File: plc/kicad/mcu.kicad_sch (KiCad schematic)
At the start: 53 parts, among them J1 Conn_01x03_Pin, J2 Conn_01x04_Pin, Q3 L8050QLT1G, Q4 L8050QLT1G, SW1 TSD003B08026A03, SW2 TSD003B08026A03, U10 ESP32-S3-MINI-1U, U11 BS-0601-SK-4W, U12 AHT20_C2757850, U13 CP2102N-A02-GQFN28R, U9 RV-3028-C7

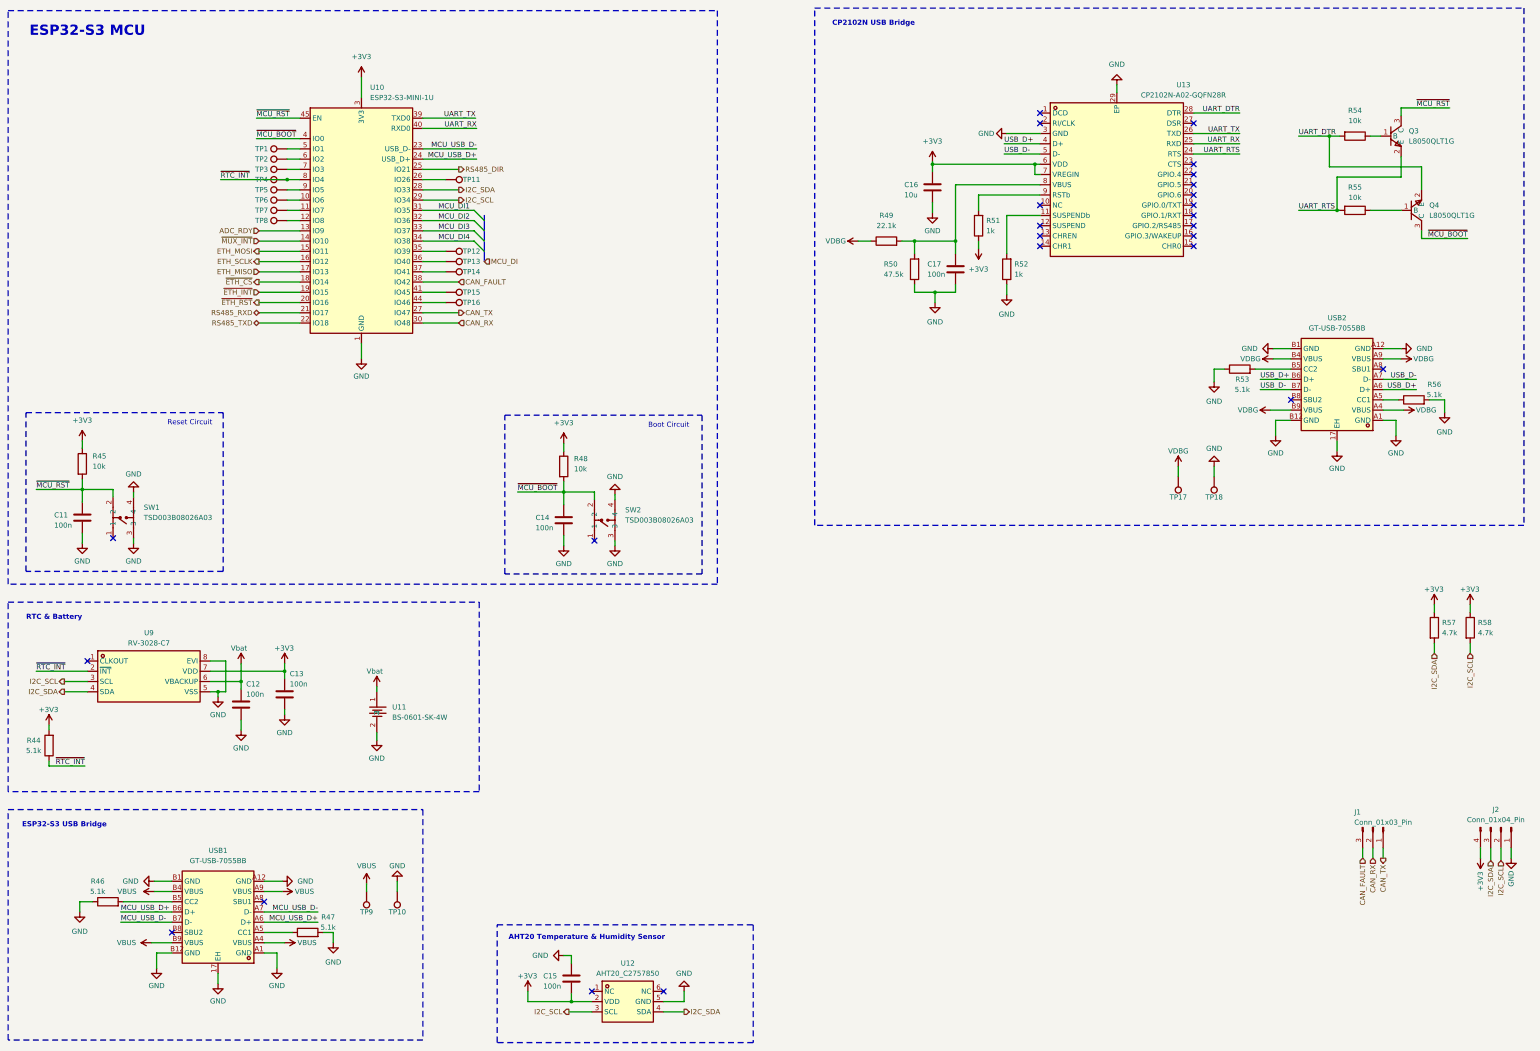
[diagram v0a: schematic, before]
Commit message: Added microSD card
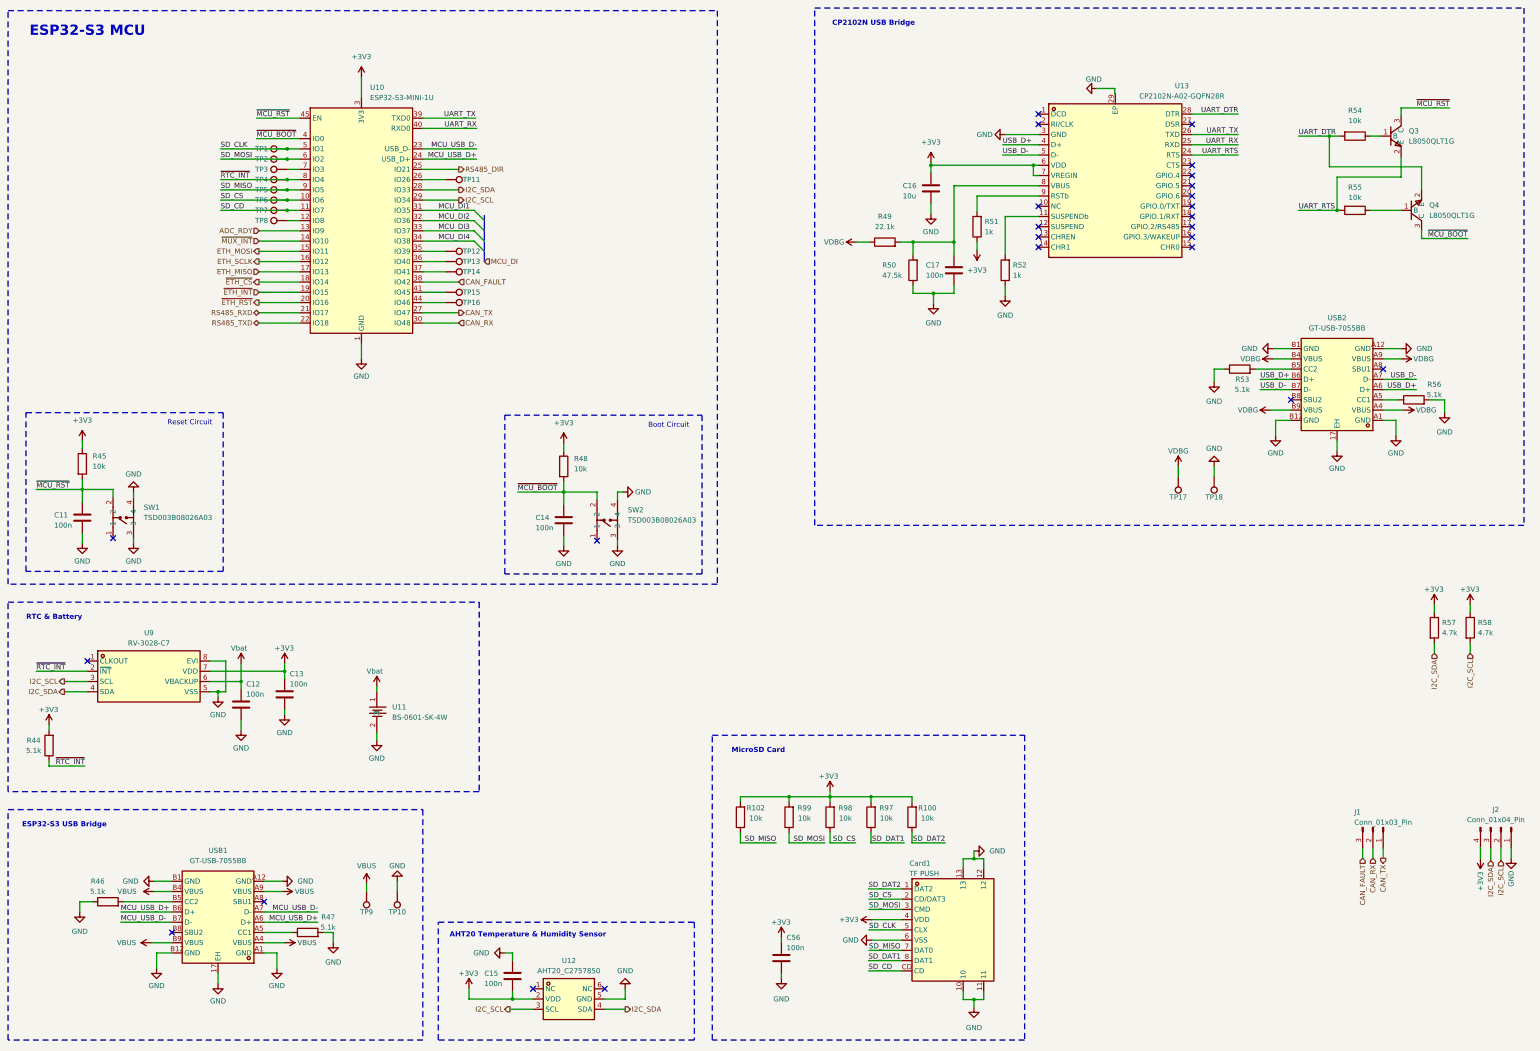
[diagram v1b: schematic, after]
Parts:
- added C56: 100n, Capacitor_SMD:C_0603_1608Metric, symbol Device:C
- added Card1: TF PUSH, LibrePLC32:TF-SMD_TF-PUSH, symbol LibrePLC32:TFPUSH
- added R100, R102, R97, R98, R99: 10k, Resistor_SMD:R_0603_1608Metric, symbol Device:R
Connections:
- net +3V3: now also C56.2, Card1.4 (VDD), R100.2, R102.2, R97.2, R98.2, R99.2
- net GND: now also C56.1, Card1.10, Card1.11, Card1.12, Card1.13, Card1.6 (VSS)
- net SD_CS: now reaches TP6.1, U10.10 (IO6)
- net SD_CS: now also Card1.2 (CD/DAT3), R98.1
- net SD_CD: now reaches TP7.1, U10.11 (IO7)
- net SD_CD: now also Card1.CD
- net SD_CLK: now reaches TP1.1, U10.5 (IO1)
- net SD_CLK: now also Card1.5 (CLX)
- net SD_MOSI: now reaches TP2.1, U10.6 (IO2)
- net SD_MOSI: now also Card1.3 (CMD), R99.1
- net SD_MISO: now reaches TP5.1, U10.9 (IO5)
- net SD_MISO: now also Card1.7 (DAT0), R102.1
- new net SD_DAT1: Card1.8 (DAT1), R97.1
- new net SD_DAT2: Card1.1 (DAT2), R100.1
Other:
- note added: "MicroSD Card"
- moved on the sheet: C15, SW2, U12

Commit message: Added setup leds & shared SPI bus
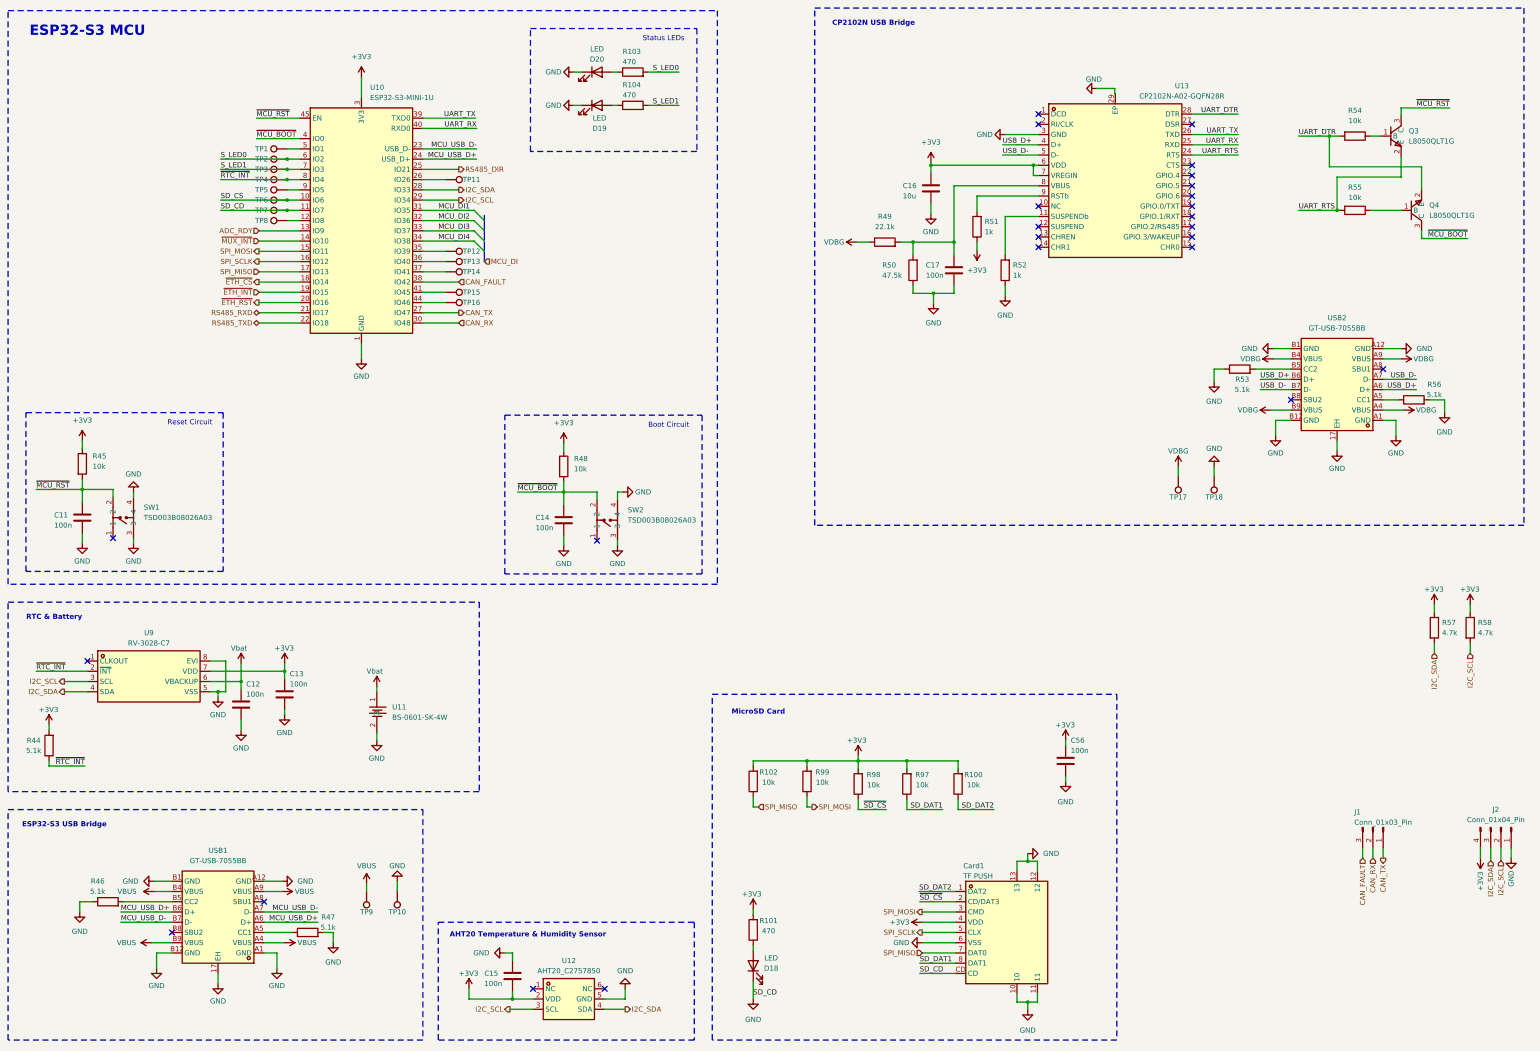
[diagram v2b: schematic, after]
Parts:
- added D18, D19, D20: LED, LED_SMD:LED_0805_2012Metric, symbol Device:LED
- added R101, R103, R104: 470, Resistor_SMD:R_0603_1608Metric, symbol Device:R
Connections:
- net SD_CD is gone; now on net GND: Card1.CD, TP7.1, U10.11 (IO7)
- net +3V3: now also R101.2
- net GND: now also D18.1 (K), D19.1 (K), D20.1 (K)
- net SD_CS: no longer Card1.2 (CD/DAT3), R98.1
- net S_LED1: now reaches TP3.1, U10.7 (IO3)
- net S_LED1: now also R104.2
- net ETH_MISO renamed SPI_MISO
- net SPI_MISO: now also Card1.7 (DAT0), R102.1
- net ETH_MOSI renamed SPI_MOSI
- net SPI_MOSI: now also Card1.3 (CMD), R99.1
- net ETH_SCLK renamed SPI_SCLK
- net SPI_SCLK: now also Card1.5 (CLX)
- net SD_CLK: no longer names the net of TP1.1, U10.5 (IO1)
- net SD_CLK: no longer Card1.5 (CLX)
- net SD_MISO: no longer names the net of TP5.1, U10.9 (IO5)
- net SD_MISO: no longer Card1.7 (DAT0), R102.1
- net SD_MOSI renamed S_LED0
- net S_LED0: now also R103.2; no longer Card1.3 (CMD), R99.1
- new net: D19.2 (A), R104.1
- new net: D18.2 (A), R101.1
- new net: D20.2 (A), R103.1
- new net ~{SD_CS}: Card1.2 (CD/DAT3), R98.1
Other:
- note added: "Status LEDs"
- moved on the sheet: C56, Card1, R100, R102, R97, R98, R99

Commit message: Fixed ADC pins & rc filter
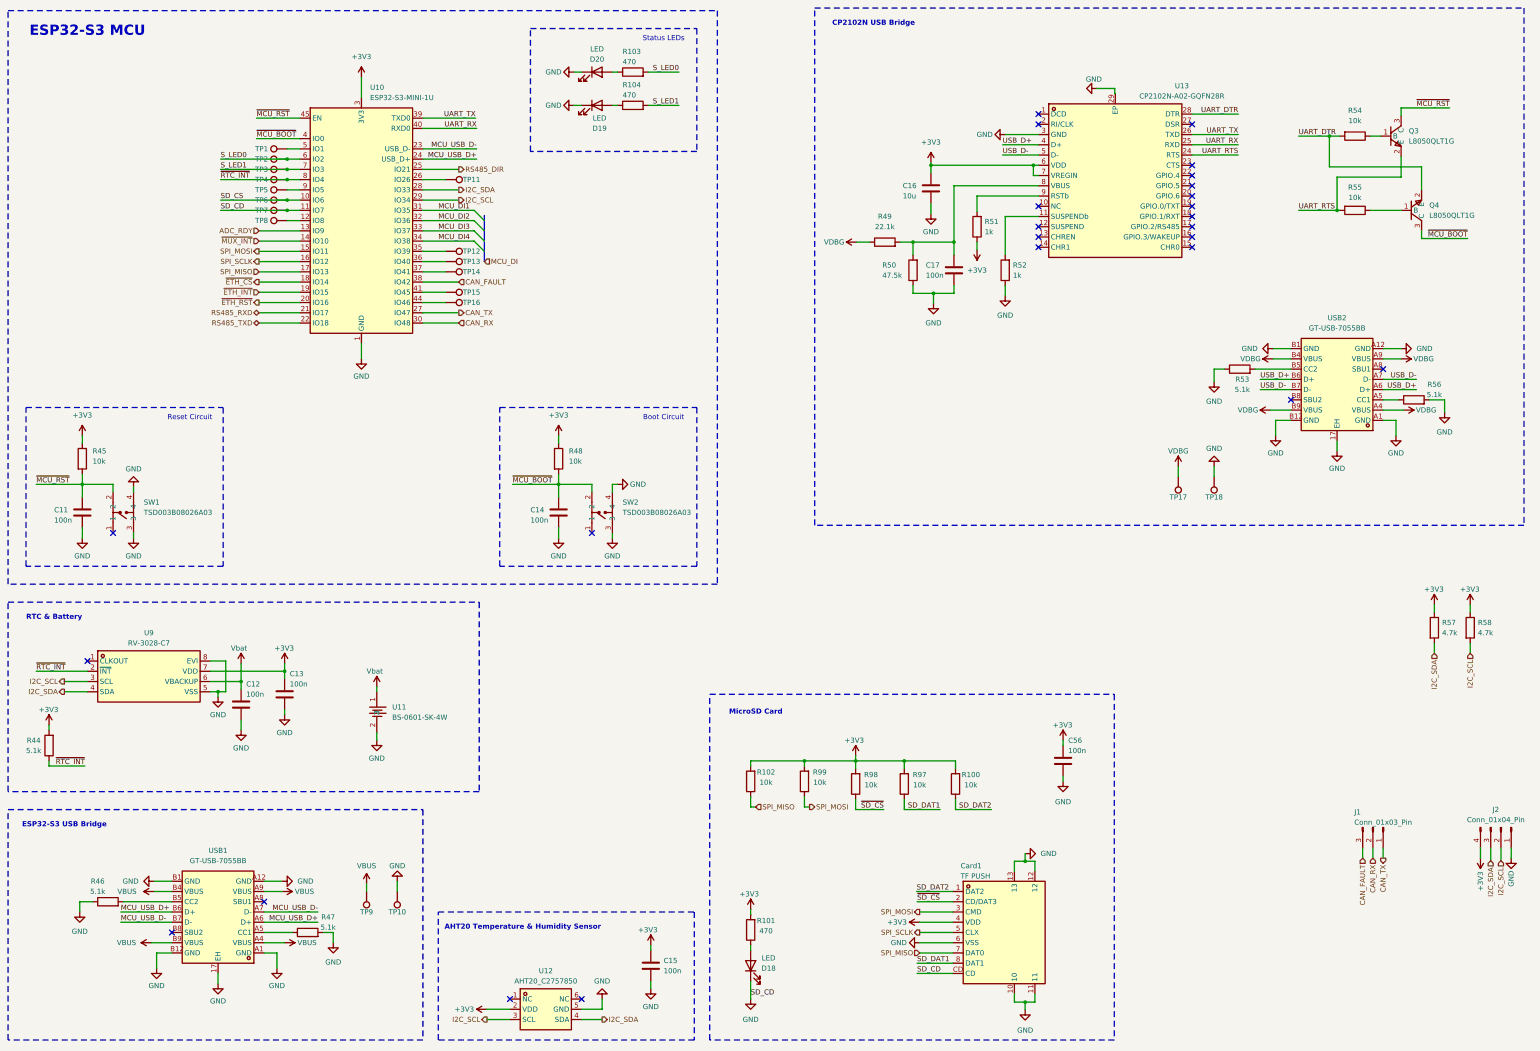
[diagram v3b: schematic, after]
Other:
- moved on the sheet: C11, C14, C56, Card1, D18, R100, R101, R102, R45, R48, R97, R98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

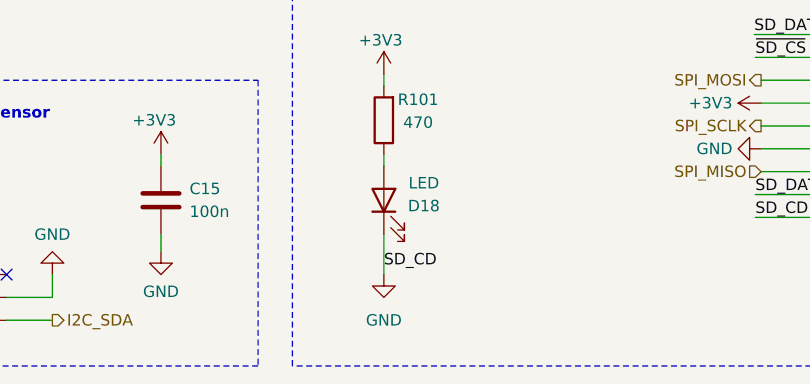
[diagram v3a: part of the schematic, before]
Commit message: SD Card PCB Placement
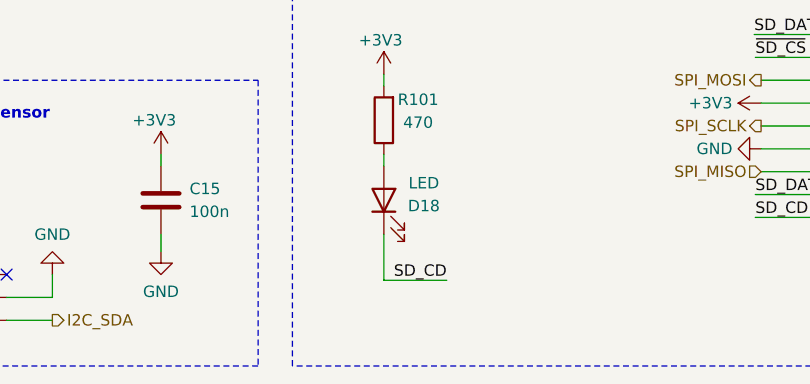
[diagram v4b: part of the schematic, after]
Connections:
- net GND: no longer Card1.CD, D18.1 (K), TP7.1, U10.11 (IO7)
- new net SD_CD: Card1.CD, D18.1 (K), TP7.1, U10.11 (IO7)
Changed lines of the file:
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@@
 	(wire
 		(pts
-			(xy 207.01 263.525) (xy 207.01 267.97)
-		)
-		(stroke
-			(width 0)
-			(type default)
-		)
-	)
-	(wire
-		(pts
 			(xy 53.975 153.67) (xy 53.975 152.4)
 		)
@@
 	(wire
 		(pts
+			(xy 207.01 268.605) (xy 207.01 263.525)
+		)
+		(stroke
+			(width 0)
+			(type default)
+		)
+	)
+	(wire
+		(pts
 			(xy 80.645 184.785) (xy 80.645 189.23)
 		)
@@
 	(wire
 		(pts
+			(xy 213.995 268.605) (xy 207.01 268.605)
+		)
+		(stroke
+			(width 0)
+			(type default)
+		)
+	)
+	(wire
+		(pts
 			(xy 103.505 254) (xy 103.505 251.46)
 		)
@@
 	)
 	(label "SD_CD"
-		(at 207.01 267.335 0)
+		(at 213.995 268.605 180)
 		(effects
 			(font
 				(size 1.27 1.27)
 			)
-			(justify left bottom)
+			(justify right bottom)
 		)
 	)
@@
 					(unit 1)
 				)
-			)
-		)
-	)
-	(symbol
-		(lib_id "power:GND")
-		(at 207.01 267.97 0)
-		(unit 1)
-		(body_style 1)
-		(exclude_from_sim no)
-		(in_bom yes)
-		(on_board yes)
-		(in_pos_files yes)
-		(dnp no)
-		(fields_autoplaced yes)
-		(property "Reference" "#PWR0255"
-			(at 207.01 274.32 0)
-			(hide yes)
-			(show_name no)
-			(do_not_autoplace no)
-			(effects
-				(font
-					(size 1.27 1.27)
-				)
-			)
-		)
-		(property "Value" "GND"
-			(at 207.01 273.05 0)
-			(show_name no)
-			(do_not_autoplace no)
-			(effects
-				(font
-					(size 1.27 1.27)
-				)
-			)
-		)
-		(property "Footprint" ""
-			(at 207.01 267.97 0)
-			(hide yes)
-			(show_name no)
-			(do_not_autoplace no)
-			(effects
-				(font
-					(size 1.27 1.27)
-				)
-			)
-		)
-		(property "Datasheet" ""
-			(at 207.01 267.97 0)
-			(hide yes)
-			(show_name no)
-			(do_not_autoplace no)
-			(effects
-				(font
-					(size 1.27 1.27)
-				)
-			)
-		)
-		(property "Description" "Power symbol creates a global label with name \"GND\" , ground"
-			(at 207.01 267.97 0)
-			(hide yes)
-			(show_name no)
-			(do_not_autoplace no)
-			(effects
-				(font
-					(size 1.27 1.27)
-				)
-			)
-		)
-		(pin "1"
-		)
-		(instances
-			(project "LibrePLC32"
-				(path "/ef4c1a27-85a3-413a-9f93-a41c4f97eee5/7ef97c26-a6eb-42fc-a9a7-66112d2bed2b"
-					(reference "#PWR0255")
-					(unit 1)
-				)
